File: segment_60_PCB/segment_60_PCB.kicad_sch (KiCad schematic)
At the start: 127 parts, among them J1 BREAKOUT, SW1 SW_Push_45deg, SW10 SW_Push_45deg, SW11 SW_Push_45deg, SW12 SW_Push_45deg, SW13 SW_Push_45deg, SW14 SW_Push_45deg, SW15 SW_Push_45deg, SW16 SW_Push_45deg, SW17 SW_Push_45deg, SW18 SW_Push_45deg, SW19 SW_Push_45deg, SW2 SW_Push_45deg, SW20 SW_Push_45deg, SW21 SW_Push_45deg, SW22 SW_Push_45deg, SW23 SW_Push_45deg, SW24 SW_Push_45deg, SW25 SW_Push_45deg, SW26 SW_Push_45deg, SW27 SW_Push_45deg, SW28 SW_Push_45deg, SW29 SW_Push_45deg, SW3 SW_Push_45deg, SW30 SW_Push_45deg, SW31 SW_Push_45deg, SW32 SW_Push_45deg, SW33 SW_Push_45deg, SW34 SW_Push_45deg, SW35 SW_Push_45deg, SW36 SW_Push_45deg, SW37 SW_Push_45deg, SW38 SW_Push_45deg, SW39 SW_Push_45deg, SW4 SW_Push_45deg, SW40 SW_Push_45deg, SW41 SW_Push_45deg, SW42 SW_Push_45deg, SW43 SW_Push_45deg, SW44 SW_Push_45deg, SW45 SW_Push_45deg, SW46 SW_Push_45deg, SW47 SW_Push_45deg, SW48 SW_Push_45deg, SW49 SW_Push_45deg, SW5 SW_Push_45deg, SW50 SW_Push_45deg, SW51 SW_Push_45deg, SW52 SW_Push_45deg, SW53 SW_Push_45deg, SW54 SW_Push_45deg, SW55 SW_Push_45deg, SW56 SW_Push_45deg, SW57 SW_Push_45deg, SW58 SW_Push_45deg, SW59 SW_Push_45deg, SW6 SW_Push_45deg, SW60 SW_Push_45deg, SW61 SW_Push_45deg, SW62 SW_Push_45deg, SW63 SW_Push_45deg, SW64 SW_Push_45deg, SW65 SW_Push_45deg, SW66 SW_Push, SW67 SW_Push, SW7 SW_Push_45deg, SW8 SW_Push_45deg, SW9 SW_Push_45deg, U1 ATmega328P-PU, U10 74HC365, U11 74HC365, U12 74HC365, U13 74HC365, U14 74HC365, U15 74HC365, U16 74HC365, U17 74HC365, U2 74HC138, U3 74HC138, U4 74HC365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

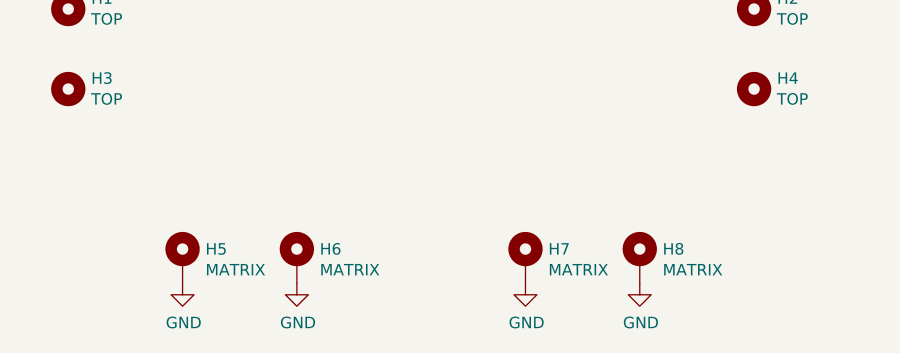
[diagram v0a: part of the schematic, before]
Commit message: Started overhauling footprint silkscreens
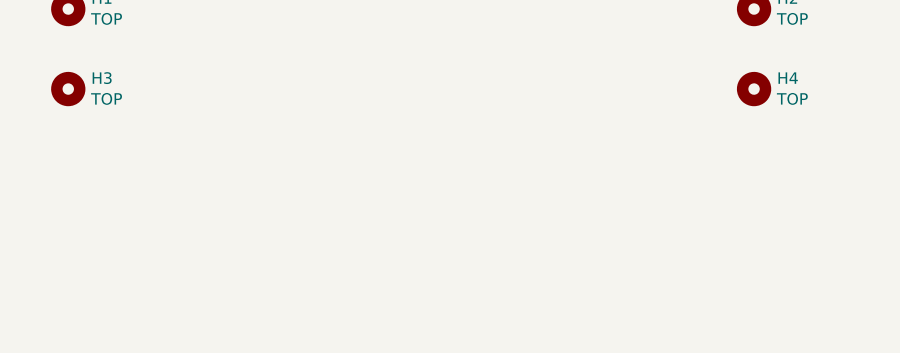
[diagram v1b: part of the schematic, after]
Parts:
- removed H5, H6, H7, H8: MATRIX, MountingHole:MountingHole_3.2mm_M3_Pad, symbol Mechanical:MountingHole_Pad
- U1: footprint Package_DIP:DIP-28_W7.62mm -> Segment_Footprints:DIP-28_W7.68mm
- U10, U11, U12, U13, U14, U15, U16, U17, U2, U3, U4, U5, U6, U7, U8, U9: footprint Package_DIP:DIP-16_W7.62mm -> Segment_Footprints:DIP-16_W7.62mm

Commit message: Updated all footprints; performing new layout
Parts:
- C4: footprint Capacitor_THT:CP_Axial_L11.0mm_D5.0mm_P18.00mm_Horizontal -> Segment_Footprints:CP_Axial_L11.0mm_D5.0mm_P18.00mm_Horizontal
- D1, D2: footprint Diode_THT:D_DO-35_SOD27_P10.16mm_Horizontal -> Segment_Footprints:D_DO-35_SOD27_P10.16mm_Horizontal
- D3, D4: footprint LED_THT:LED_D5.0mm -> Segment_Footprints:LED_D5.0mm
- J1: footprint Connector_IDC:IDC-Header_2x06_P2.54mm_Vertical -> Segment_Footprints:IDC-Header_2x06_P2.54mm_Vertical
- R1, R2, R3, R4, R5, R6, R7, R8: footprint Resistor_THT:R_Axial_DIN0207_L6.3mm_D2.5mm_P10.16mm_Horizontal -> Segment_Footprints:R_Axial_L6.3mm_D2.5mm_P10.16mm_Horizontal
- RN1: footprint Resistor_THT:R_Array_SIP7 -> Segment_Footprints:R_Array_SIP7
- SW66, SW67: footprint Button_Switch_THT:SW_PUSH_6mm -> Segment_Footprints:SW_PUSH_6mm
